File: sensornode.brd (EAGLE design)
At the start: 112.3 x 63.5 mm, 75 parts, among them IC1 CP2104, Q1 mmbt2222, Q2 mmbt2222, Q3 DMG3415U, SW2 KMR2, U1 TSL2591, U2 AP2112-3.3, U3 MCP73831T-2ACI/OT, U4 BMEx80, X2 ESP32_WROOM32_SKINNY, X4 20329

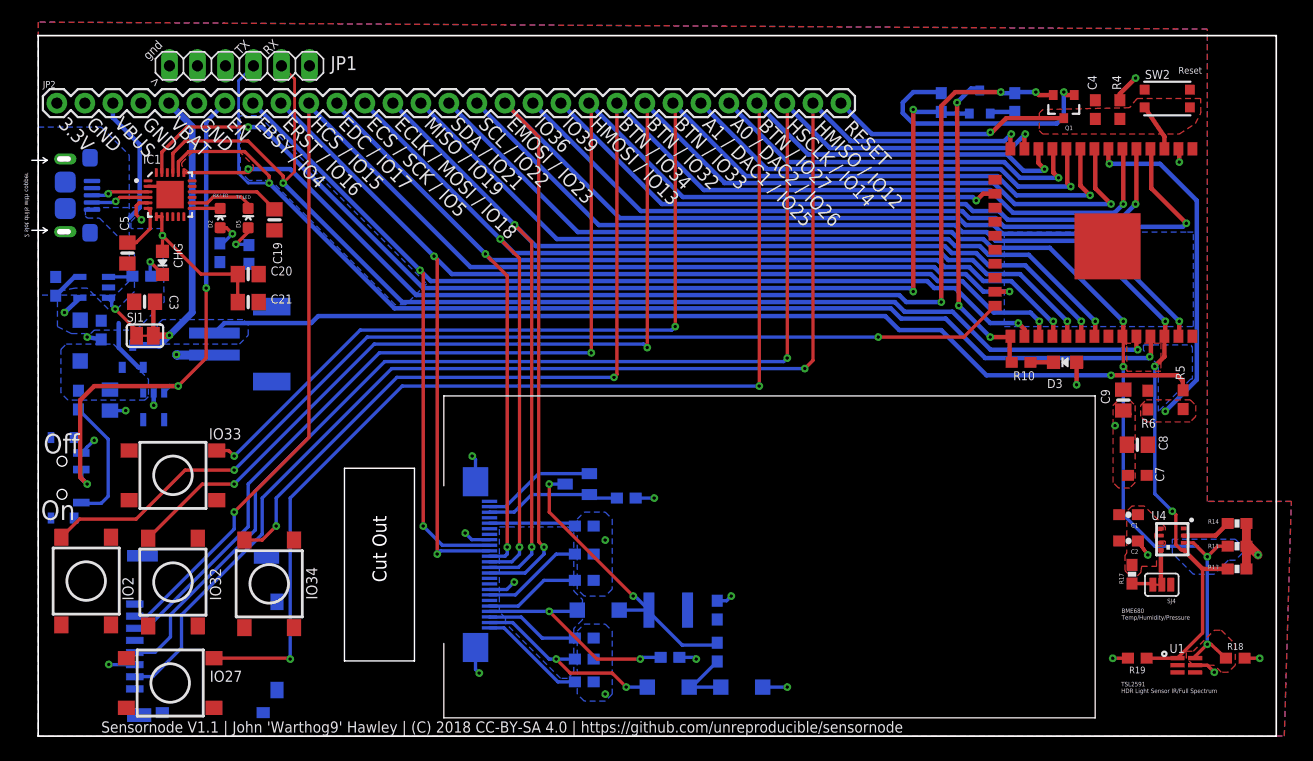
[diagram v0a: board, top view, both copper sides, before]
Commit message: Adjusting e-ink screen, and reving to v1.2
So this adds C22, a 1uF cap on VGL and R20 to EINK_GDR.  These
fall in line with what's on the waveshare and Open Hardware Summit
badge and should be slightly more reliable than my current circuit
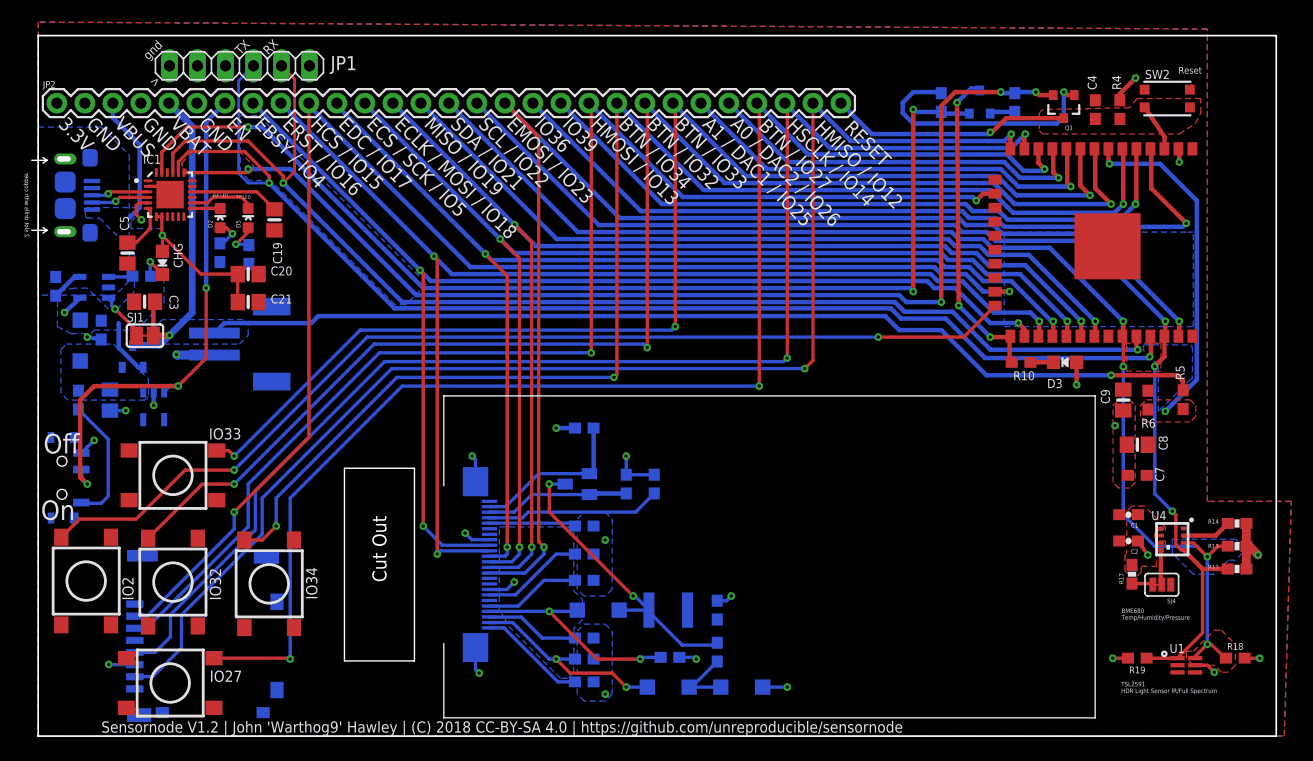
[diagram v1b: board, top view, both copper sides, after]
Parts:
- added C22: 1uF, SparkFun-Capacitors:0603-CAP
- added R20: 10K, SparkFun-Resistors:0603-RES
- moved R16 1.27 mm to (53.3, 22.9), turned to 90 degrees
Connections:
- new net N$24: C22.1, U$15.4-VGL
- net EINK_GDR: now also R20.1
- net GND: now also C22.2, R20.2
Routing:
- net N$24: track 0.00 -> 15.9 mm
- net EINK_GDR: track 10.3 -> 14.6 mm
- net GND: track 30.9 -> 35.1 mm, vias 16 -> 17
- net EINK_RESE: track 12.3 -> 13.4 mm
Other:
- board text added: "Sensornode V1.2 | John 'Warthog9' Hawley | (C) 2018 CC-BY-SA 4.0 | https://github.com/unreproducible/sensornode"
- board text removed: "Sensornode V1.1 John 'Warthog9' Hawley | (C) 2018 CC-BY-SA 4.0 https://github.com/unreproducible/sensornode"
- board text removed: "Sensornode V1.1 | John 'Warthog9' Hawley | (C) 2018 CC-BY-SA 4.0 | https://github.com/unreproducible/sensornode"
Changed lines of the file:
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@@
 Temp/Humidity/Pressure</text>
 <text x="13.97" y="54.2925" size="0.4064" layer="26" rot="MR270">Disable Serial 3.3V</text>
-<text x="5.715" y="0.3175" size="1.016" layer="21">Sensornode V1.1 | John 'Warthog9' Hawley | (C) 2018 CC-BY-SA 4.0 | https://github.com/unreproducible/sensornode</text>
+<text x="5.715" y="0.3175" size="1.016" layer="21">Sensornode V1.2 | John 'Warthog9' Hawley | (C) 2018 CC-BY-SA 4.0 | https://github.com/unreproducible/sensornode</text>
 <text x="98.235" y="3.90375" size="0.4064" layer="21">TSL2591
 HDR Light Sensor IR/Full Spectrum</text>
@@
 <text x="0.238125" y="19.605625" size="1.778" layer="21">On</text>
 <text x="0.47625" y="25.638125" size="1.778" layer="21">Off</text>
-<text x="110.31375" y="1.984375" size="1.016" layer="22" rot="MR0">                    Sensornode V1.1
-John 'Warthog9' Hawley | (C) 2018 CC-BY-SA 4.0
-https://github.com/unreproducible/sensornode</text>
+<text x="97.31375" y="1.984375" size="1.016" layer="22" rot="MR0">Sensornode V1.2 | John 'Warthog9' Hawley | (C) 2018 CC-BY-SA 4.0 | https://github.com/unreproducible/sensornode</text>
 <text x="15.478125" y="26.908125" size="1.016" layer="21">IO33</text>
 <text x="25.320625" y="12.3825" size="1.016" layer="21" rot="R90">IO34</text>
@@
 <attribute name="VALUE" x="52.07" y="24.765" size="1.27" layer="28" rot="MR270"/>
 </element>
-<element name="R16" library="SparkFun-Resistors" package="0603-RES" value="2.2" x="53.34" y="21.59" rot="MR180">
-<attribute name="PROD_ID" value="RES-07857" x="53.34" y="21.59" size="1.778" layer="28" rot="MR180" display="off"/>
+<element name="R16" library="SparkFun-Resistors" package="0603-RES" value="2.2" x="53.34" y="22.86" rot="MR90">
+<attribute name="PROD_ID" value="RES-07857" x="53.34" y="22.86" size="1.778" layer="28" rot="MR90" display="off"/>
 </element>
 <element name="U$15" library="Warthog9-Screens" package="WAVSHARE-BUYDISPLAY-2.13-THM" value="WAVSHARE-BUYDISPLAY-2.132.13-THROUGH" x="36.67125" y="22.5425" smashed="yes" rot="R180"/>
@@
 <element name="SD1" library="we-con" package="SD_5031821853" value="SD-CARD-MSD50" x="7.958125" y="8.13125" rot="MR90">
 <attribute name="DIGIKEY" value="WM9750TR-ND" x="7.958125" y="8.13125" size="1.778" layer="28" rot="MR90" display="off"/>
+</element>
+<element name="R20" library="SparkFun-Resistors" package="0603-RES" value="10K" x="49.53" y="27.94" rot="MR0">
+<attribute name="PROD_ID" value="RES-07857" x="49.53" y="27.94" size="1.778" layer="28" rot="MR0" display="off"/>
+</element>
+<element name="C22" library="SparkFun-Capacitors" package="0603-CAP" value="1uF" x="55.88" y="22.86" rot="MR90">
+<attribute name="PROD_ID" value="CAP-08604" x="55.88" y="22.86" size="1.778" layer="28" rot="MR90" display="off"/>
 </element>
 </elements>
@@
 <wire x1="65.7175" y1="4.445" x2="67.945" y2="4.445" width="0.3048" layer="16"/>
 <via x="67.945" y="4.445" extent="1-16" drill="0.3048"/>
-<wire x1="54.19" y1="21.59" x2="55.88" y2="21.59" width="0.3048" layer="16"/>
-<via x="55.88" y="21.59" extent="1-16" drill="0.3048"/>
+<wire x1="53.34" y1="23.71" x2="53.34" y2="25.4" width="0.3048" layer="16"/>
+<via x="53.34" y="25.4" extent="1-16" drill="0.3048"/>
 <wire x1="61.595" y1="12.28" x2="62.445" y2="12.28" width="0.3048" layer="16"/>
 <wire x1="62.445" y1="12.28" x2="62.865" y2="12.7" width="0.3048" layer="16"/>
@@
 <wire x1="6.3801" y1="40.7035" x2="8.702" y2="39.40175" width="0" layer="19" extent="1-16"/>
 <wire x1="1.5875" y1="41.64875" x2="2.4558" y2="45.75375" width="0" layer="19" extent="16-16"/>
+<contactref element="R20" pad="2"/>
+<contactref element="C22" pad="2"/>
+<wire x1="48.68" y1="27.94" x2="46.99" y2="27.94" width="0.4064" layer="16"/>
+<via x="46.99" y="27.94" extent="1-16" drill="0.3048"/>
+<wire x1="55.88" y1="23.71" x2="53.34" y2="23.71" width="0.3048" layer="16"/>
 </signal>
 <signal name="TXLED">
@@
 <wire x1="42.4053" y1="20.8153" x2="45.4" y2="23.81" width="0.3048" layer="16"/>
 <wire x1="45.4" y1="23.81" x2="49.995" y2="23.81" width="0.3048" layer="16"/>
+<contactref element="R20" pad="1"/>
+<wire x1="50.38" y1="27.94" x2="50.38" y2="24.195" width="0.4064" layer="16"/>
+<wire x1="50.38" y1="24.195" x2="49.995" y2="23.81" width="0.4064" layer="16"/>
 </signal>
 <signal name="EINK_RESE">
@@
 <wire x1="40.95115" y1="20.32" x2="40.93845" y2="20.3073" width="0.3048" layer="16"/>
 <wire x1="49.995" y1="21.91" x2="50.315" y2="21.59" width="0.3048" layer="16"/>
-<wire x1="50.315" y1="21.59" x2="52.49" y2="21.59" width="0.3048" layer="16"/>
+<wire x1="50.315" y1="21.59" x2="50.735" y2="22.01" width="0.4064" layer="16"/>
+<wire x1="50.735" y1="22.01" x2="53.34" y2="22.01" width="0.4064" layer="16"/>
 </signal>
 <signal name="N$14">
@@
 </polygon>
 </signal>
+<signal name="N$24">
+<contactref element="U$15" pad="4-VGL"/>
+<contactref element="C22" pad="1"/>
+<wire x1="40.93845" y1="19.7993" x2="43.9293" y2="19.7993" width="0.3048" layer="16"/>
+<wire x1="43.9293" y1="19.7993" x2="44.45" y2="20.32" width="0.3048" layer="16"/>
+<wire x1="44.45" y1="20.32" x2="54.19" y2="20.32" width="0.3048" layer="16"/>
+<wire x1="54.19" y1="20.32" x2="55.88" y2="22.01" width="0.3048" layer="16"/>
+</signal>
 </signals>

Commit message: Removing the backup FTDI port
As it turns out my luck with the power changes to the serial port
chip worked just fine, and as a result the FTDI header is actually
extraneous and obnoxious.  Remove it, get the board a little
smaller.
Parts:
- removed JP1: (no value), pinhead:1X06
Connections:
- net GND: no longer JP1.1
- net RXD0: no longer JP1.5
- net TXD0: no longer JP1.4
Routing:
- net TXD0: track 113.1 -> 111.2 mm
- net RXD0: track 110.8 -> 109.2 mm
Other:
- board size 112.3 x 63.5 mm -> 112.3 x 61 mm
- board text removed: "RX"
- board text removed: "TX"
- board text removed: "gnd"
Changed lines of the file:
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@@
 <board>
 <plain>
-<wire x1="112.3" y1="0" x2="112.3" y2="63.54" width="0.1524" layer="20"/>
-<wire x1="112.3" y1="63.54" x2="0" y2="63.54" width="0.1524" layer="20"/>
-<wire x1="0" y1="63.54" x2="0" y2="0" width="0.1524" layer="20"/>
+<wire x1="112.3" y1="0" x2="112.3" y2="61" width="0.1524" layer="20"/>
+<wire x1="112.3" y1="61" x2="0" y2="61" width="0.1524" layer="20"/>
+<wire x1="0" y1="61" x2="0" y2="0" width="0.1524" layer="20"/>
 <wire x1="0" y1="0" x2="112.3" y2="0" width="0.1524" layer="20"/>
 <text x="17.93875" y="48.73625" size="0.3048" layer="21">TX LED</text>
@@
 <text x="70.32625" y="55.08625" size="1.27" layer="21" rot="R315">HMISO / IO12</text>
 <text x="73.025" y="55.08625" size="1.27" layer="21" rot="R315">RESET</text>
-<text x="10.00125" y="61.2775" size="0.8128" layer="21" rot="R45">gnd</text>
-<text x="18.335625" y="61.75375" size="0.8128" layer="21" rot="R45">TX</text>
-<text x="20.875625" y="61.75375" size="0.8128" layer="21" rot="R45">RX</text>
 <text x="10.556875" y="58.816875" size="0.8128" layer="21" rot="R45">&gt;</text>
 <text x="0.238125" y="19.605625" size="1.778" layer="21">On</text>
@@
 <element name="C21" library="microbuilder" package="0805-NO" value="0.1uF" x="19.05" y="39.37"/>
 <element name="C5" library="microbuilder" package="0805-NO" value="10uF" x="8.09625" y="43.815" rot="R90"/>
-<element name="JP1" library="pinhead" package="1X06" value="" x="18.25625" y="60.80125" smashed="yes">
-<attribute name="NAME" x="26.514425" y="60.40755" size="1.27" layer="25" ratio="10"/>
-<attribute name="VALUE" x="10.63625" y="57.62625" size="1.27" layer="27"/>
-</element>
 <element name="SD1" library="we-con" package="SD_5031821853" value="SD-CARD-MSD50" x="7.958125" y="8.13125" rot="MR90">
 <attribute name="DIGIKEY" value="WM9750TR-ND" x="7.958125" y="8.13125" size="1.778" layer="28" rot="MR90" display="off"/>
@@
 <wire x1="39.66845" y1="25.10155" x2="39.37" y2="25.4" width="0.3048" layer="16"/>
 <contactref element="C5" pad="1"/>
-<contactref element="JP1" pad="1"/>
 <contactref element="SD1" pad="GND"/>
 <wire x1="8.758125" y1="6.48125" x2="6.4" y2="6.48125" width="0.3048" layer="16"/>
@@
 <via x="46.99" y="27.94" extent="1-16" drill="0.3048"/>
 <wire x1="55.88" y1="23.71" x2="53.34" y2="23.71" width="0.3048" layer="16"/>
+<wire x1="100.3675" y1="58.6325" x2="104.4675" y2="58.6325" width="0" layer="19" extent="1-1"/>
+<wire x1="95.885" y1="57.6825" x2="100.3675" y2="58.6325" width="0" layer="19" extent="1-1"/>
+<wire x1="104.695" y1="53.2675" x2="104.4675" y2="58.6325" width="0" layer="19" extent="1-1"/>
+<wire x1="97.17625" y1="44.60875" x2="104.695" y2="53.2675" width="0" layer="19" extent="1-1"/>
+<wire x1="104.695" y1="36.2675" x2="96.995" y2="44.4275" width="0" layer="19" extent="1-1"/>
+<wire x1="100.6475" y1="31.33" x2="104.695" y2="36.2675" width="0" layer="19" extent="1-1"/>
+<wire x1="98.425" y1="31.43" x2="100.6475" y2="31.33" width="0" layer="19" extent="1-1"/>
+<wire x1="100.6525" y1="26.4325" x2="100.6475" y2="31.33" width="0" layer="19" extent="1-1"/>
+<wire x1="100.5525" y1="23.655" x2="100.6525" y2="26.4325" width="0" layer="19" extent="1-1"/>
+<wire x1="98.05125" y1="20.0825" x2="100.5525" y2="23.655" width="0" layer="19" extent="1-1"/>
+<wire x1="98.05125" y1="17.70125" x2="98.05125" y2="20.0825" width="0" layer="19" extent="1-1"/>
+<wire x1="101.845" y1="18.185" x2="98.05125" y2="17.70125" width="0" layer="19" extent="1-1"/>
+<wire x1="103.895" y1="18.835" x2="101.845" y2="18.185" width="0" layer="19" extent="1-1"/>
+<wire x1="102.7303" y1="13.7325" x2="101.845" y2="18.185" width="0" layer="19" extent="1-1"/>
+<wire x1="103.34" y1="5.78" x2="102.7303" y2="13.7325" width="0" layer="19" extent="1-1"/>
+<wire x1="86.795" y1="50.4675" x2="95.885" y2="57.6825" width="0" layer="19" extent="1-1"/>
+<wire x1="67.945" y1="4.445" x2="98.05125" y2="17.70125" width="0" layer="19" extent="1-1"/>
+<wire x1="59.69" y1="6.985" x2="65.7175" y2="4.445" width="0" layer="19" extent="16-16"/>
+<wire x1="61.595" y1="12.28" x2="59.53125" y2="7.14375" width="0" layer="19" extent="16-16"/>
+<wire x1="51.435" y1="3.81" x2="58.15875" y2="7.14375" width="0" layer="19" extent="16-16"/>
+<wire x1="50.38" y1="4.92125" x2="51.435" y2="3.81" width="0" layer="19" extent="16-16"/>
+<wire x1="50.38" y1="6.985" x2="50.38" y2="4.92125" width="0" layer="19" extent="16-16"/>
+<wire x1="50.38" y1="8.89" x2="50.38" y2="6.985" width="0" layer="19" extent="16-16"/>
+<wire x1="50.38" y1="14.12875" x2="50.38" y2="8.89" width="0" layer="19" extent="16-16"/>
+<wire x1="50.38" y1="16.51" x2="50.38" y2="14.12875" width="0" layer="19" extent="16-16"/>
+<wire x1="51.435" y1="17.78" x2="50.38" y2="16.51" width="0" layer="19" extent="16-16"/>
+<wire x1="50.38" y1="19.05" x2="51.435" y2="17.78" width="0" layer="19" extent="16-16"/>
+<wire x1="53.34" y1="23.71" x2="50.38" y2="19.05" width="0" layer="19" extent="16-16"/>
+<wire x1="48.68" y1="27.94" x2="53.34" y2="25.4" width="0" layer="19" extent="16-16"/>
+<wire x1="43.18" y1="13.97" x2="50.38" y2="14.12875" width="0" layer="19" extent="16-16"/>
+<wire x1="40.93845" y1="17.8181" x2="43.18" y2="13.97" width="0" layer="19" extent="16-16"/>
+<wire x1="39.66845" y1="23.0759" x2="38.735" y2="18.415" width="0" layer="19" extent="16-16"/>
+<wire x1="39.66845" y1="8.0391" x2="40.93845" y2="13.2969" width="0" layer="19" extent="16-16"/>
+<wire x1="23.205" y1="17.78625" x2="38.735" y2="18.415" width="0" layer="19" extent="1-16"/>
+<wire x1="16.19875" y1="21.40375" x2="23.205" y2="17.78625" width="0" layer="19" extent="1-1"/>
+<wire x1="14.47375" y1="17.945" x2="16.19875" y2="21.40375" width="0" layer="19" extent="1-1"/>
+<wire x1="7.56" y1="16.6" x2="14.47375" y2="17.945" width="0" layer="19" extent="1-16"/>
+<wire x1="6.60200625" y1="18.037990625" x2="7.56" y2="16.6" width="0" layer="19" extent="1-16"/>
+<wire x1="3.909" y1="25.6815" x2="6.60200625" y2="18.037990625" width="0" layer="19" extent="1-16"/>
+<wire x1="6.50875" y1="29.53" x2="5.08" y2="26.82875" width="0" layer="19" extent="16-16"/>
+<wire x1="10.4775" y1="30.00375" x2="7.9375" y2="29.5275" width="0" layer="19" extent="16-16"/>
+<wire x1="12.58875" y1="34.56" x2="10.4775" y2="31.30385" width="0" layer="19" extent="16-16"/>
+<wire x1="8.702" y1="39.40175" x2="12.54125" y2="34.6075" width="0" layer="19" extent="1-16"/>
+<wire x1="6.3801" y1="40.7035" x2="8.702" y2="39.40175" width="0" layer="19" extent="1-16"/>
+<wire x1="8.09625" y1="42.865" x2="6.3801" y2="40.7035" width="0" layer="19" extent="1-16"/>
+<wire x1="4.7038" y1="45.65375" x2="8.09625" y2="42.865" width="0" layer="19" extent="1-16"/>
+<wire x1="2.4558" y1="45.75375" x2="4.7038" y2="45.65375" width="0" layer="19" extent="16-16"/>
+<wire x1="2.4558" y1="47.85375" x2="2.4558" y2="45.75375" width="0" layer="19" extent="16-16"/>
+<wire x1="2.4558" y1="50.25375" x2="2.4558" y2="47.85375" width="0" layer="19" extent="16-16"/>
+<wire x1="2.4558" y1="52.35375" x2="2.4558" y2="50.25375" width="0" layer="19" extent="16-16"/>
+<wire x1="4.7038" y1="52.45375" x2="2.4558" y2="52.35375" width="0" layer="19" extent="16-16"/>
+<wire x1="4.8808" y1="50.35375" x2="4.7038" y2="52.45375" width="0" layer="19" extent="16-16"/>
+<wire x1="1.5875" y1="41.64875" x2="2.4558" y2="45.75375" width="0" layer="19" extent="16-16"/>
+<wire x1="5.715" y1="35.98" x2="8.702" y2="39.40175" width="0" layer="19" extent="1-16"/>
+<wire x1="4.235" y1="57.41625" x2="4.7038" y2="52.45375" width="0" layer="19" extent="16-16"/>
+<wire x1="9.315" y1="57.41625" x2="4.235" y2="57.41625" width="0" layer="19" extent="1-1"/>
+<wire x1="14.395" y1="57.41625" x2="9.315" y2="57.41625" width="0" layer="19" extent="1-1"/>
+<wire x1="9.96484375" y1="49.867246875" x2="4.8808" y2="50.35375" width="0" layer="19" extent="1-16"/>
+<wire x1="20" y1="39.37" x2="15.985" y2="34.56" width="0" layer="19" extent="1-16"/>
+<wire x1="20" y1="41.91" x2="20" y2="39.37" width="0" layer="19" extent="1-1"/>
+<wire x1="21.43125" y1="45.88125" x2="20" y2="41.91" width="0" layer="19" extent="1-1"/>
+<wire x1="10.96" y1="6.5" x2="7.56" y2="16.6" width="0" layer="19" extent="16-16"/>
+<wire x1="8.46" y1="3.4" x2="10.96" y2="6.5" width="0" layer="19" extent="16-16"/>
+<wire x1="6.8" y1="4.3" x2="8.46" y2="3.4" width="0" layer="19" extent="16-16"/>
+<wire x1="15.947009375" y1="2.566971875" x2="10.96" y2="6.5" width="0" layer="19" extent="1-16"/>
 </signal>
 <signal name="TXLED">
@@
 <wire x1="99.742625" y1="35.04565" x2="99.615" y2="35.173275" width="0.4064" layer="1"/>
 <wire x1="99.615" y1="35.173275" x2="99.615" y2="36.2675" width="0.4064" layer="1"/>
-<contactref element="JP1" pad="5"/>
-<wire x1="22.06625" y1="60.80125" x2="23.256875" y2="59.610625" width="0.254" layer="1"/>
 <wire x1="23.256875" y1="59.610625" x2="23.256875" y2="51.196875" width="0.254" layer="1"/>
 <wire x1="23.256875" y1="51.196875" x2="22.225" y2="50.165" width="0.254" layer="1"/>
@@
 <wire x1="100.93315" y1="36.31565" x2="100.93315" y2="34.5185" width="0.4064" layer="1"/>
 <wire x1="100.93315" y1="34.5185" x2="100.8253" y2="34.41065" width="0.4064" layer="1"/>
-<contactref element="JP1" pad="4"/>
 <wire x1="18.176875" y1="51.038125" x2="19.05" y2="50.165" width="0.254" layer="16"/>
 <wire x1="20.955" y1="50.165" x2="19.05" y2="50.165" width="0.254" layer="16"/>
-<wire x1="18.176875" y1="59.451875" x2="19.52625" y2="60.80125" width="0.254" layer="16"/>
 <wire x1="18.176875" y1="51.038125" x2="18.176875" y2="59.451875" width="0.254" layer="16"/>
 <wire x1="12.71484375" y1="52.08484375" x2="13.6525" y2="53.0225" width="0.3048" layer="1"/>
